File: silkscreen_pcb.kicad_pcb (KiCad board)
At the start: 2 copper layers, 60 x 111.3 mm, 188 parts, among them J1 USB_C_Receptacle, J2 FH34SRJ-24S-0.5SH_50_, J3 FH34SRJ-6S-0.5SH_50_, J4 FH34SRJ-6S-0.5SH_50_, J5 Conn_01x02, J6 PPPC062LJBN-RC, J7 Micro_SD_Card, Q1 FS8205A, Q2 AO3401A, Q3 AO3401A, Q4 IRLML6346TRPBF, Q5 BSS138, Q6 BSS138, Q7 AO3401A, Q8 AO3401A, Q9 BSS138, SW1 SW_Push, SW10 SW_Push, SW11 SW_Push, SW2 SW_Push, SW3 SW_Push, SW4 SW_Push, SW5 SW_Push, SW6 SW_Push, SW7 SW_Push, SW8 SW_Push, SW9 SW_Push, U1 TPD4E1U06DBVR, U10 TPS923610DRLR, U11 TP4056-42-ESOP8, U12 74LVC1G04, U13 DS3231MZ, U14 RV-8263-C7, U2 TPS2116DRL, U3 TLV75533PDBV, U4 ESP32-S3-WROOM-1, U5 DW01A, U6 TPD4E1U06DBVR, U7 TPD4E1U06DBVR, U8 TPD4E1U06DBVR, U9 TPD4E1U06DBVR

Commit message: Cut-down board keeps 3V3 on the charge-enable switch; silkscreen wording
- Cutting the board at y 62 for the 3.68" (x3) build removed both 3V3 feeds
  to the charge-enable switch (Q2/R81), so the TP4056 CE pin stayed low and
  a cut board never charged. A new 3V3 trace on B.Cu, below the cut, joins
  the two feeds. PWR_BUTTON and LED_SW are rerouted around it, one GND via
  moved, and the pour is refilled. DRC of a copy trimmed at y 62 shows no
  unconnected 3V3.
- Welcome text on F.SilkS: "maximizing cost-savings and simplicity".
- Gerbers, drill files and netlist.ipc regenerated with the Fabrication
  Toolkit. Placement and BOM files are unchanged.

Boards made from earlier files, including the 2026-09-21 order, don't have
this trace. If one is cut down, add one wire from a retained 3V3 point to
Q2 pad 2 or R81 pad 2: bridge the two cut 3V3 stubs at the edge (x 87.53
and 100.60, y 62), or run it from R40 pad 2 to R81 pad 2. Then check that
CE reads 3V3 with a correctly oriented cell fitted.

D3 and D8 (frontlight ESD clamps) stay above the cut, so on a cut board the
LED nets at J3 have no clamp. Accepted: with no dev header, nothing gets
plugged into the LED pins while the board is powered.
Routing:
- net 3V3: track 385.4 -> 401.0 mm
- net PWR_BUTTON: track 87.2 -> 86.4 mm
- net LED_SW: track 180.4 -> 179.7 mm

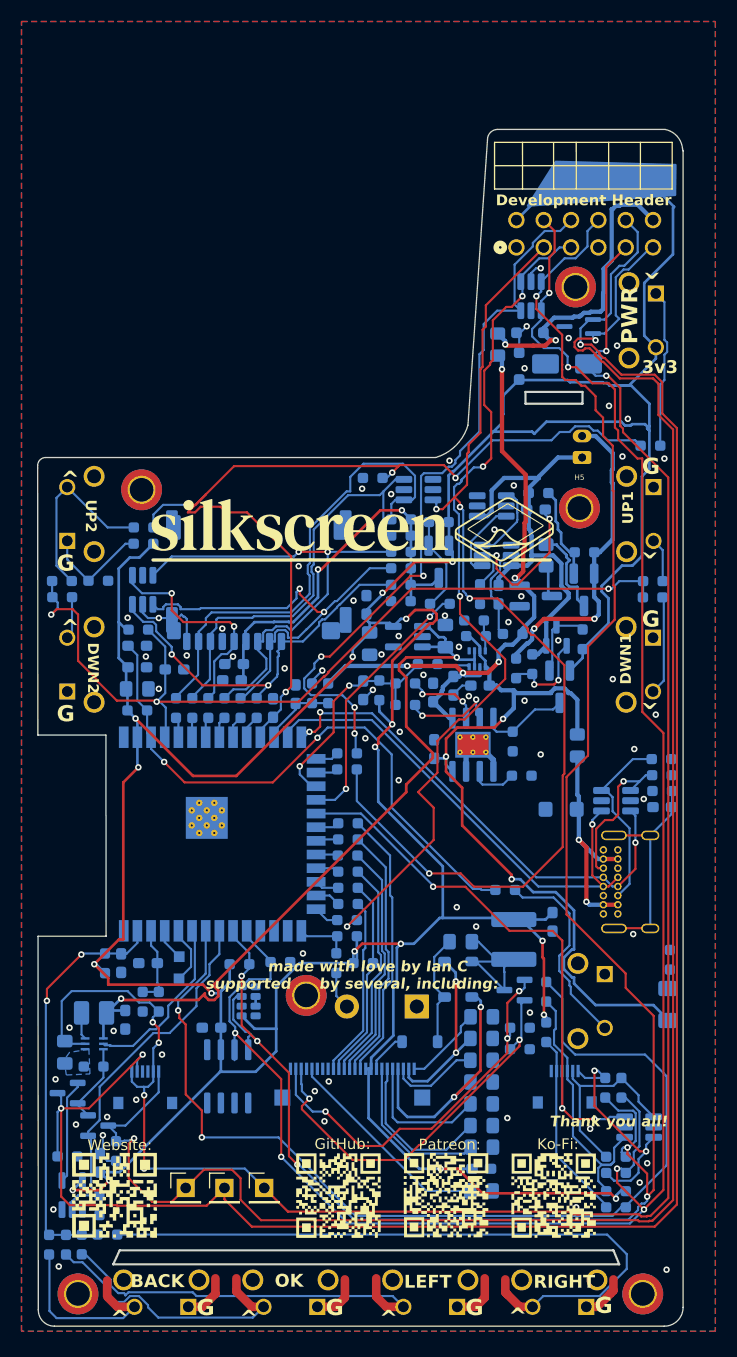
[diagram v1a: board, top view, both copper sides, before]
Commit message: Rev 1.01: GND stitching vias below the cut line, revision label, docs and plots
- Five GND stitching vias below the cut line join the power-section ground
  (U3, U2, Q1, so the battery return) to the main ground. A board cut down for
  a smaller display no longer depends on one microSD shell tab for ground. A
  copy trimmed at y 62 shows no unconnected items.
- Title blocks (PCB and schematic) set to Rev 1.01, 2026-09-30. The Gerber zip
  is now Silkscreen_Reader_PCB_1.01.zip; the Rev 1.0 zip that was ordered stays
  in history at aeb5b39.
- Track tidy-up: collinear segments merged, redundant stubs removed, the 1 um
  3V3 stub from 3edd0c8 gone, and the B+ track beside J5 moved from x 97.7 to
  x 97.1. The front-button solder-bridge tabs that the cleanup had deleted are
  restored unchanged.
- Gerbers, drill files and netlist.ipc regenerated with the Fabrication Toolkit
  and checked against a fresh kicad-cli export. BOM and placement unchanged.
- README, HARDWARE.md and fabrication/README.md: zip name, revision, the
  cut-down section (a board made before 1.01 needs a 3V3 wire and a GND wire),
  and a Rev 1.0 order record with its SHA-256. Schematic and layout PDFs
  re-plotted. The 2026-09-30 audit notes the finished 1.01 items.
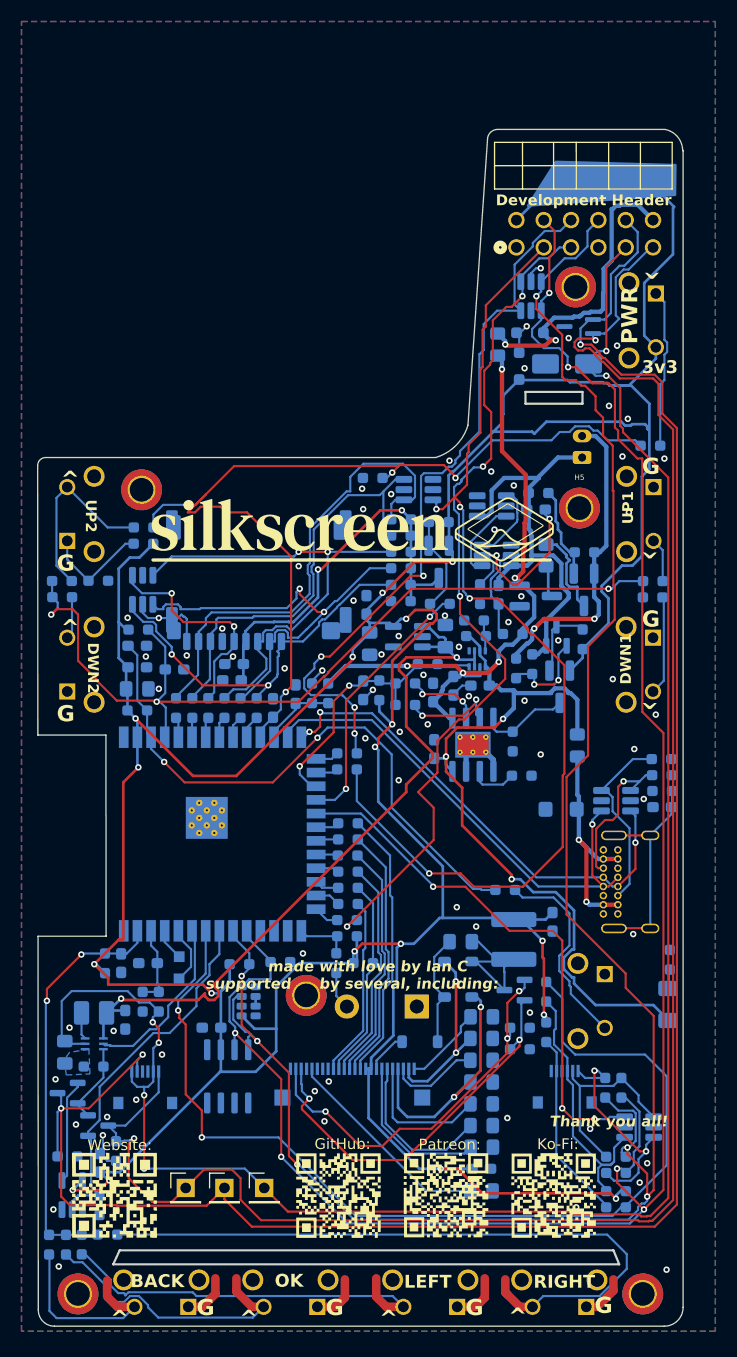
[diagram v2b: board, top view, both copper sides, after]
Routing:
- net I2C_SDA: track 181.9 -> 180.9 mm
- net B+: track 29.5 -> 28.9 mm
- net GND: vias 69 -> 74
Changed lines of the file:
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@@
 	(title_block
 		(title "Silkscreen Reader PCB")
-		(date "2026-09-12")
-		(rev "1.0")
+		(date "2026-09-30")
+		(rev "1.01")
 		(company "idc LLC")
 		(comment 1 "Open-hardware e-reader base board")
@@
 	)
 	(segment
-		(start 87.4 60)
-		(end 87.4 59.3)
-		(width 0.4)
-		(layer "F.Cu")
-		(net 3)
-	)
-	(segment
 		(start 87.4 66.9)
-		(end 87.4 60)
+		(end 87.4 59.3)
 		(width 0.4)
 		(layer "F.Cu")
@@
 	)
 	(segment
-		(start 101.001 64.9)
-		(end 101.101 65)
-		(width 0.25)
-		(layer "B.Cu")
-		(net 6)
-	)
-	(segment
 		(start 53.510001 93.5)
 		(end 53.510001 91.932499)
@@
 	)
 	(segment
-		(start 101.101 68.561462)
-		(end 101.101 64.6)
-		(width 0.25)
-		(layer "B.Cu")
-		(net 6)
-	)
-	(segment
 		(start 76.974801 82.874801)
 		(end 77.3 83.2)
@@
 	)
 	(segment
-		(start 89 60.25)
-		(end 89.2 60.45)
-		(width 0.25)
-		(layer "B.Cu")
-		(net 6)
-	)
-	(segment
 		(start 87.526 61.724)
 		(end 89 60.25)
@@
 	)
 	(segment
-		(start 101.101 64.6)
+		(start 101.101 68.561462)
 		(end 101.101 62.501)
 		(width 0.25)
@@
 	)
 	(segment
-		(start 94.569654 137.851)
-		(end 94.030346 137.851)
-		(width 0.2)
-		(layer "F.Cu")
-		(net 11)
-	)
-	(segment
 		(start 98.4 61.03781)
 		(end 98.4 64.56219)
@@
 	)
 	(segment
-		(start 100.130346 137.851)
-		(end 94.4 137.851)
+		(start 94.030346 137.851)
+		(end 100.130346 137.851)
 		(width 0.2)
 		(layer "F.Cu")
@@
 	)
 	(segment
+		(start 96.492787 76.307213)
+		(end 95.983578 76.307213)
+		(width 0.4)
+		(layer "B.Cu")
+		(net 49)
+	)
+	(segment
 		(start 96 82.5)
 		(end 96.4 82.1)
@@
 	)
 	(segment
-		(start 97.7 69.908496)
-		(end 97.7 75.1)
-		(width 0.4)
-		(layer "B.Cu")
-		(net 49)
-	)
-	(segment
-		(start 97.7 67.1)
-		(end 97.7 68.591504)
+		(start 94.850003 65.499999)
+		(end 96.099999 65.499999)
 		(width 0.4)
 		(layer "B.Cu")
@@
 	)
 	(segment
-		(start 97.7 75.1)
-		(end 96.492787 76.307213)
-		(width 0.4)
-		(layer "B.Cu")
-		(net 49)
-	)
-	(segment
-		(start 97.611462 69.819958)
-		(end 97.7 69.908496)
-		(width 0.4)
-		(layer "B.Cu")
-		(net 49)
-	)
-	(segment
-		(start 97.7 68.591504)
-		(end 97.611462 68.680042)
+		(start 97.1 66.5)
+		(end 97.1 75.7)
 		(width 0.4)
 		(layer "B.Cu")
@@
 	(segment
 		(start 96.099999 65.499999)
-		(end 97.7 67.1)
+		(end 97.1 66.5)
 		(width 0.4)
 		(layer "B.Cu")
@@
 	)
 	(segment
-		(start 94.850003 65.499999)
-		(end 96.099999 65.499999)
-		(width 0.4)
-		(layer "B.Cu")
-		(net 49)
-	)
-	(segment
 		(start 89.724 84.776)
 		(end 88.714286 85.785714)
@@
 	)
 	(segment
-		(start 96.492787 76.307213)
-		(end 95.983578 76.307213)
+		(start 97.1 75.7)
+		(end 96.492787 76.307213)
 		(width 0.4)
 		(layer "B.Cu")
@@
 	)
 	(segment
-		(start 97.611462 68.680042)
-		(end 97.611462 69.819958)
-		(width 0.4)
-		(layer "B.Cu")
-		(net 49)
-	)
-	(segment
 		(start 86.61928 75.65)
 		(end 88.8 73.46928)
@@
 	(segment
 		(start 96.25 146.45)
-		(end 97.5 145.2)
+		(end 97.763462 144.936538)
 		(width 0.8)
 		(layer "F.Cu")
@@
 	)
 	(segment
-		(start 97.5 145.2)
-		(end 97.763462 144.936538)
-		(width 0.8)
-		(layer "F.Cu")
-		(net 72)
-	)
-	(segment
 		(start 83.237462 146.45)
 		(end 84.95 146.45)
@@
 	)
 	(via
+		(at 74.5 72.3)
+		(size 0.6)
+		(drill 0.3)
+		(layers "F.Cu" "B.Cu")
+		(free yes)
+		(net 72)
+	)
+	(via
 		(at 58.1 85.9)
 		(size 0.6)
@@
 	)
 	(via
+		(at 80.5 92.3)
+		(size 0.6)
+		(drill 0.3)
+		(layers "F.Cu" "B.Cu")
+		(free yes)
+		(net 72)
+	)
+	(via
 		(at 77.9 93)
 		(size 0.6)
@@
 	)
 	(via
+		(at 86.4 68.8)
+		(size 0.6)
+		(drill 0.3)
+		(layers "F.Cu" "B.Cu")
+		(free yes)
+		(net 72)
+	)
+	(via
 		(at 76.2 85.8)
 		(size 0.6)
@@
 	)
 	(via
+		(at 99.2 72.6)
+		(size 0.6)
+		(drill 0.3)
+		(layers "F.Cu" "B.Cu")
+		(free yes)
+		(net 72)
+	)
+	(via
 		(at 47.8 129.5)
 		(size 0.6)
@@
 	)
 	(via
+		(at 81.6 74.5)
+		(size 0.6)
+		(drill 0.3)
+		(layers "F.Cu" "B.Cu")
+		(free yes)
+		(net 72)
+	)
+	(via
 		(at 82.1 82.2)
 		(size 0.6)
@@
 	(segment
 		(start 62.54 122.55)
-		(end 62.54 123.524999)
-		(width 0.2)
-		(layer "B.Cu")
-		(net 99)
-	)
-	(segment
-		(start 62.54 122.55)
 		(end 62.54 121.06)
 		(width 0.2)
@@
 	)
 	(segment
-		(start 63.81 122.55)
-		(end 63.9 122.46)
-		(width 0.2)
-		(layer "B.Cu")
-		(net 102)
-	)
-	(segment
 		(start 62.424 119.75899)
 		(end 62.424 117.901001)
@@
 	)
 	(segment
-		(start 90.3 57.1)
+		(start 87.814028 57.1)
 		(end 91.426325 57.1)
 		(width 0.4)
@@
 		(net 133)
 	)
-	(segment
-		(start 90.3 57.1)
-		(end 87.814028 57.1)
-		(width 0.4)
-		(layer "F.Cu")
-		(net 133)
-	)
 	(via
 		(at 87.703466 56.989438)
@@
 		(layer "B.Cu")
 		(net 134)
-	)
-	(segment
-		(start 87.081362 81.106739)
-		(end 87.358344 81.106739)
-		(width 0.4)
-		(layer "B.Cu")
-		(net 134)
